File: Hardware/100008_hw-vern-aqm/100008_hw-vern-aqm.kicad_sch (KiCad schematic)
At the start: 0 parts

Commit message: schematic work
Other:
- removed sheet Block Diagram
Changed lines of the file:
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@@
-		)
-	)
-	(text_box "Metadata can be set in File → Schematic Setup → Project → Text Variables"
-		(exclude_from_sim no)
-		(at 8.89 300.99 0)
-		(size 119.38 6.35)
-		(stroke
-			(width -0.0001)
-			(type default)
-		)
-		(fill
-			(type none)
-		)
-		(effects
-			(font
-				(size 2.54 2.54)
-				(thickness 0.381)
-				(bold yes)
-				(color 0 0 0 1)
-			)
-			(justify right top)
 		)
 	)
@@
 			(justify right bottom)
 			(href "#17")
-		)
-	)
-	(sheet
-		(at 299.72 302.26)
-		(size 35.56 5.08)
-		(stroke
-			(width 0.1524)
-			(type solid)
-		)
-		(fill
-			(color 0 0 0 0.0000)
-		)
-		(property "Sheetname" "Block Diagram"
-			(at 299.72 301.2309 0)
-			(effects
-				(font
-					(face "Times New Roman")
-					(size 1.905 1.905)
-					(bold yes)
-					(color 0 0 0 1)
-				)
-				(justify left bottom)
-			)
-		)
-		(property "Sheetfile" "Block Diagram.kicad_sch"
-			(at 300.99 303.53 0)
-			(effects
-				(font
-					(face "Arial")
-					(size 1.27 1.27)
-				)
-				(justify left top)
-			)
-		)
-		(instances
-			(project "100008_hw-vern-aqm"
-				(path "/0650c7a8-acba-429c-9f8e-eec0baf0bc1c"
-					(page "2")
-				)
-			)
 		)
 	)
@@
 			(project "100008_hw-vern-aqm"
 				(path "/0650c7a8-acba-429c-9f8e-eec0baf0bc1c"
-					(page "7")
+					(page "6")
 				)
 			)
@@
 	)
 	(sheet
-		(at 299.72 313.69)
+		(at 299.72 302.26)
 		(size 35.56 5.08)
 		(stroke
@@
 		)
 		(property "Sheetname" "Project Architecture"
-			(at 299.72 312.6609 0)
+			(at 299.72 301.2309 0)
 			(effects
 				(font
@@
 		)
 		(property "Sheetfile" "Project Architecture.kicad_sch"
-			(at 300.99 314.96 0)
+			(at 300.99 303.53 0)
 			(effects
 				(font
@@
 			(project "100008_hw-vern-aqm"
 				(path "/0650c7a8-acba-429c-9f8e-eec0baf0bc1c"
-					(page "3")
+					(page "2")
 				)
 			)

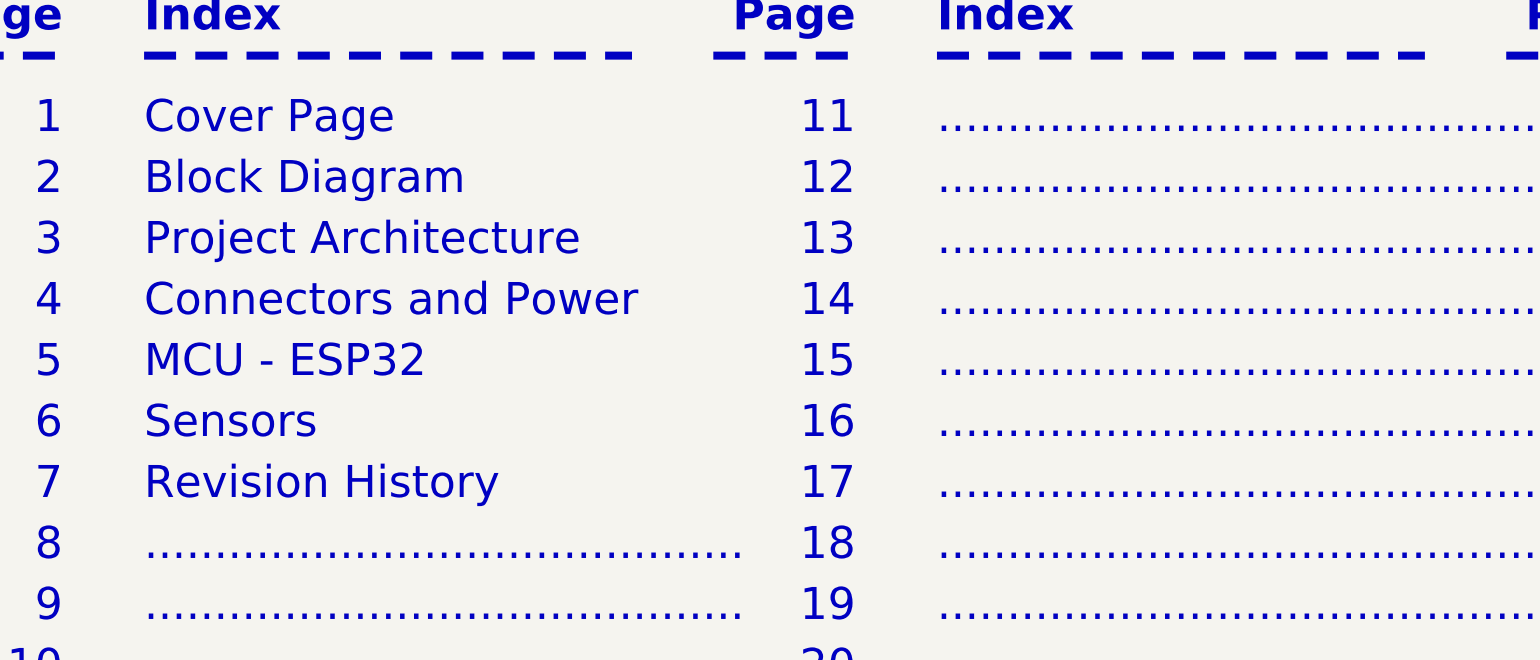
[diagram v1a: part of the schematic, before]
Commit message: PCB routing and DRC fixes
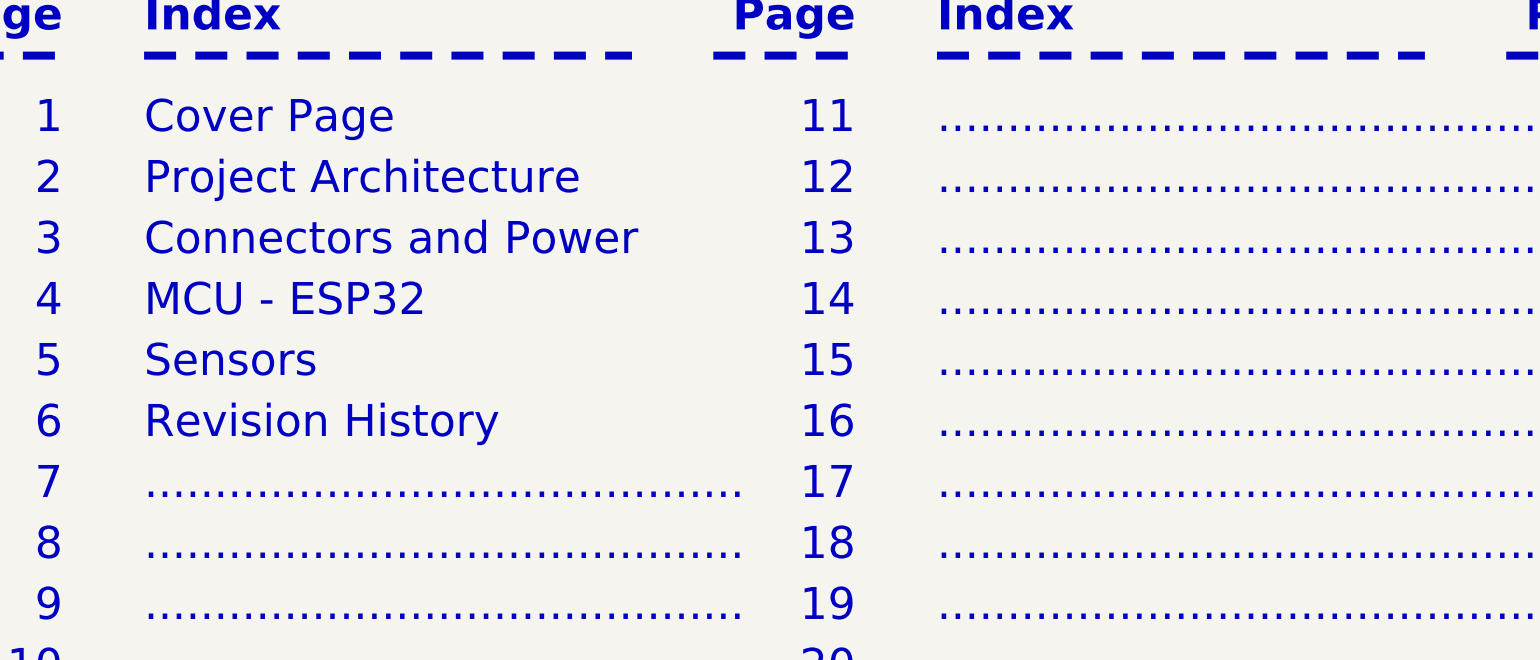
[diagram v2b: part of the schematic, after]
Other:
- note removed: "Block Diagram"
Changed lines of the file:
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@@
 	(text "Connectors and Power"
 		(exclude_from_sim no)
-		(at 45.72 106.68 0)
-		(effects
-			(font
-				(face "Times New Roman")
-				(size 4 4)
-				(color 0 0 0 1)
-			)
-			(justify left bottom)
-			(href "#4")
+		(at 45.72 99.06 0)
+		(effects
+			(font
+				(face "Times New Roman")
+				(size 4 4)
+				(color 0 0 0 1)
+			)
+			(justify left bottom)
+			(href "#3")
 		)
 	)
@@
 	(text "MCU - ESP32"
 		(exclude_from_sim no)
-		(at 45.72 114.3 0)
-		(effects
-			(font
-				(face "Times New Roman")
-				(size 4 4)
-				(color 0 0 0 1)
-			)
-			(justify left bottom)
-			(href "#5")
+		(at 45.72 106.68 0)
+		(effects
+			(font
+				(face "Times New Roman")
+				(size 4 4)
+				(color 0 0 0 1)
+			)
+			(justify left bottom)
+			(href "#4")
 		)
 	)
@@
 			(justify left bottom)
 			(href "#28")
+		)
+	)
+	(text "..........................................."
+		(exclude_from_sim no)
+		(at 45.72 129.54 0)
+		(effects
+			(font
+				(face "Times New Roman")
+				(size 4 4)
+				(color 0 0 0 1)
+			)
+			(justify left bottom)
+			(href "#7")
 		)
 	)
@@
 	(text "Sensors"
 		(exclude_from_sim no)
-		(at 45.72 121.92 0)
-		(effects
-			(font
-				(face "Times New Roman")
-				(size 4 4)
-				(color 0 0 0 1)
-			)
-			(justify left bottom)
-			(href "#6")
+		(at 45.72 114.3 0)
+		(effects
+			(font
+				(face "Times New Roman")
+				(size 4 4)
+				(color 0 0 0 1)
+			)
+			(justify left bottom)
+			(href "#5")
 		)
 	)
@@
 		)
 	)
-	(text "Block Diagram"
+	(text "Project Architecture"
 		(exclude_from_sim no)
 		(at 45.72 91.44 0)
@@
 		)
 	)
-	(text "Project Architecture"
-		(exclude_from_sim no)
-		(at 45.72 99.06 0)
-		(effects
-			(font
-				(face "Times New Roman")
-				(size 4 4)
-				(color 0 0 0 1)
-			)
-			(justify left bottom)
-			(href "#3")
-		)
-	)
 	(text "CHECKED - There shouldn't be any mistakes. Contact the engineer if you find any."
 		(exclude_from_sim no)
@@
 	(text "Revision History"
 		(exclude_from_sim no)
-		(at 45.72 129.54 0)
-		(effects
-			(font
-				(face "Times New Roman")
-				(size 4 4)
-				(color 0 0 0 1)
-			)
-			(justify left bottom)
-			(href "#7")
-		)
-	)
+		(at 45.72 121.92 0)
+		(effects
+			(font
+				(face "Times New Roman")
+				(size 4 4)
+				(color 0 0 0 1)
+			)
+			(justify left bottom)
+			(href "#6")
+		)
+	)

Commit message: schematic release, pcb release
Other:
- note added: "Board designed for 3.5" LCD display with ILI9488 driver"
- note removed: "Add a comment here"
